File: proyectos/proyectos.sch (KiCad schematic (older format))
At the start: 54 parts, among them P1 CONN_01X06, P2 CONN_01X03, P3 CONN_01X05, P4 CONN_01X04, SW1 SW_PUSH, U1 AD8232_A, U2 ADP3339, U3 PIC16F688, Y1 Crystal_8MHz

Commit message: version ECG 1.4
INCORPORACION DE PIC Y REGULADOR
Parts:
- removed C8, C9: 1uF, Capacitors_SMD:C_0805_HandSoldering, symbol 1uF
- removed JP2, JP3, JP?: JUMPER, symbol JUMPER
- removed P1: CONN_01X06, Huellas:Pin_Header_Straight_1x06_Pitch2.54mm, symbol CONN_01X06
- removed P4: CONN_01X04, Pin_Headers:Pin_Header_Straight_1x04_Pitch2.54mm, symbol CONN_01X04
- removed R16, R17, R21, R25: 000, Resistors_SMD:R_0805_HandSoldering, symbol 000
- removed SW1: SW_PUSH, Huellas:SWICHT_KPT-1187B, symbol SW_PUSH
- removed U2: ADP3339, TO_SOT_Packages_SMD:SOT-223-3Lead_TabPin2, symbol ADP3339
- added C14, C9: 0.1uF, Capacitors_SMD:C_0805_HandSoldering, symbol 0.1uF
- added C15: 4.7uF, Capacitors_SMD:C_0805_HandSoldering, symbol 4.7uF
- added C8: 10uF, Capacitors_SMD:C_0805_HandSoldering, symbol 10uF
- added JP2: LATIDOS_ECG, Pin_Headers:Pin_Header_Straight_1x02_Pitch2.54mm, symbol LATIDOS_ECG
- added JP3: RESET_PIC, Pin_Headers:Pin_Header_Straight_1x02_Pitch2.54mm, symbol RESET_PIC
- added JP4: PASO_A/D, Pin_Headers:Pin_Header_Straight_1x02_Pitch2.54mm, symbol PASO_A/D
- added JP5: ALIMENT_PIC-KIT, Pin_Headers:Pin_Header_Straight_1x02_Pitch2.54mm, symbol ALIMENT_PIC-KIT
- added P1, P6: CONN_01X02, Pin_Headers:Pin_Header_Straight_1x02_Pitch2.54mm, symbol CONN_01X02
- added P4: CONN_01X03, Pin_Headers:Pin_Header_Straight_1x03_Pitch2.54mm, symbol CONN_01X03
- added P5: CONN_01X03, Huellas:Pin_Header_Straight_1x03_Pitch2.54mm, symbol CONN_01X03-RESCUE-proyectos
- added U2: ADP3303-3.3, Housings_SOIC:SOIC-8_3.9x4.9mm_Pitch1.27mm, symbol ADP3303-3.3
- JP1: value JUMPER3 -> ALIMEN_PIC; footprint (none) -> Pin_Headers:Pin_Header_Straight_1x03_Pitch2.54mm
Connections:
- net labels added: SDN_OFF, VCC, VCC_PIC
- net labels removed: 3V3, 3V_REG, Vpp
- wire segments 145 -> 147
- no-connect marks 0 -> 1
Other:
- note added: "ALIMENTACION\n"
- note added: "ANALOGICAS\n"
- note added: "DIGITALES\n"
- note added: "ENTRADA DE CONTROL\n DE APAGADO DEL ECG"
- note added: "IND. ALIMENTACION\n"
- note added: "OPCION DE ALIMENTACION DEL PIC\n\n"
- note added: "REGULADOR DE 3.3V\n"
- note added: "RESET"
- note removed: "IND. PIC16F688"
- note removed: "OPCION DE ALIMENTACION ECG\n"
- note removed: "REGULADOR DE 3V\n"
- note removed: "SALIDAS ANALOGICAS\n"
- moved on the sheet: C10, JP1, P2, P3, R19, R20, R22

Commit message: version ECG 1.5
MODIFICACION DE PAD TORNILLOS
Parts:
- P5: footprint Huellas:Pin_Header_Straight_1x03_Pitch2.54mm -> Pin_Headers:Pin_Header_Straight_1x03_Pitch2.54mm
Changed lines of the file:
@@
 F 0 "P5" H 4800 7450 50  0000 C CNN
 F 1 "CONN_01X03" V 4900 7250 50  0000 C CNN
-F 2 "Huellas:Pin_Header_Straight_1x03_Pitch2.54mm" H 4800 7250 50  0001 C CNN
+F 2 "Pin_Headers:Pin_Header_Straight_1x03_Pitch2.54mm" H 4800 7250 50  0001 C CNN
 F 3 "" H 4800 7250 50  0000 C CNN
 	1    4800 7250

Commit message: VERSION 1.7 ECG Y PIC
NUEVA VERSION
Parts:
- added P7, P8: CONN_01X01, Huellas:MountingHole_1.8mm_Pad, symbol CONN_01X01
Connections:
- net GND: now also P4.1 (P1); no longer P4.3 (P3)
- net O_DIG1: now also P4.2 (P2); no longer P4.1 (P1)
- net O_DIG2: now also P4.3 (P3); no longer P4.2 (P2)
- no-connect marks 1 -> 3
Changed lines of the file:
@@
 Text GLabel 8100 4250 0    47   Input ~ 0
 ADC
-Text Label 6250 6800 3    47   ~ 0
-GND
-Text Label 6350 6800 3    47   ~ 0
+Text Label 6450 6700 3    47   ~ 0
+GND
+Text Label 6250 6700 3    47   ~ 0
 O_DIG2
-Text Label 6450 6800 3    47   ~ 0
+Text Label 6350 6700 3    47   ~ 0
 O_DIG1
 Text Label 9950 3850 2    47   ~ 0
@@
 	9150 3550 9150 3700
 Wire Wire Line
-	6250 6950 6250 6800
-Wire Wire Line
-	6350 6950 6350 6800
-Wire Wire Line
-	6450 6950 6450 6800
+	6250 6700 6250 6950
+Wire Wire Line
+	6350 6700 6350 6950
+Wire Wire Line
+	6450 6700 6450 6950
 Wire Wire Line
 	8100 4400 7650 4400
@@
 	0    1    1    0
 $EndComp
+$Comp
+L CONN_01X01 P8
+U 1 1 591B656B
+P 10300 5900
+F 0 "P8" H 10300 6000 50  0000 C CNN
+F 1 "CONN_01X01" V 10400 5900 50  0000 C CNN
+F 2 "Huellas:MountingHole_1.8mm_Pad" H 10300 5900 50  0001 C CNN
+F 3 "" H 10300 5900 50  0000 C CNN
+	1    10300 5900
+	1    0    0    -1
+$EndComp
+$Comp
+L CONN_01X01 P7
+U 1 1 591B6624
+P 9350 5900
+F 0 "P7" H 9350 6000 50  0000 C CNN
+F 1 "CONN_01X01" V 9450 5900 50  0000 C CNN
+F 2 "Huellas:MountingHole_1.8mm_Pad" H 9350 5900 50  0001 C CNN
+F 3 "" H 9350 5900 50  0000 C CNN
+	1    9350 5900
+	1    0    0    -1
+$EndComp
+NoConn ~ 10100 5900
+NoConn ~ 9150 5900
 $EndSCHEMATC

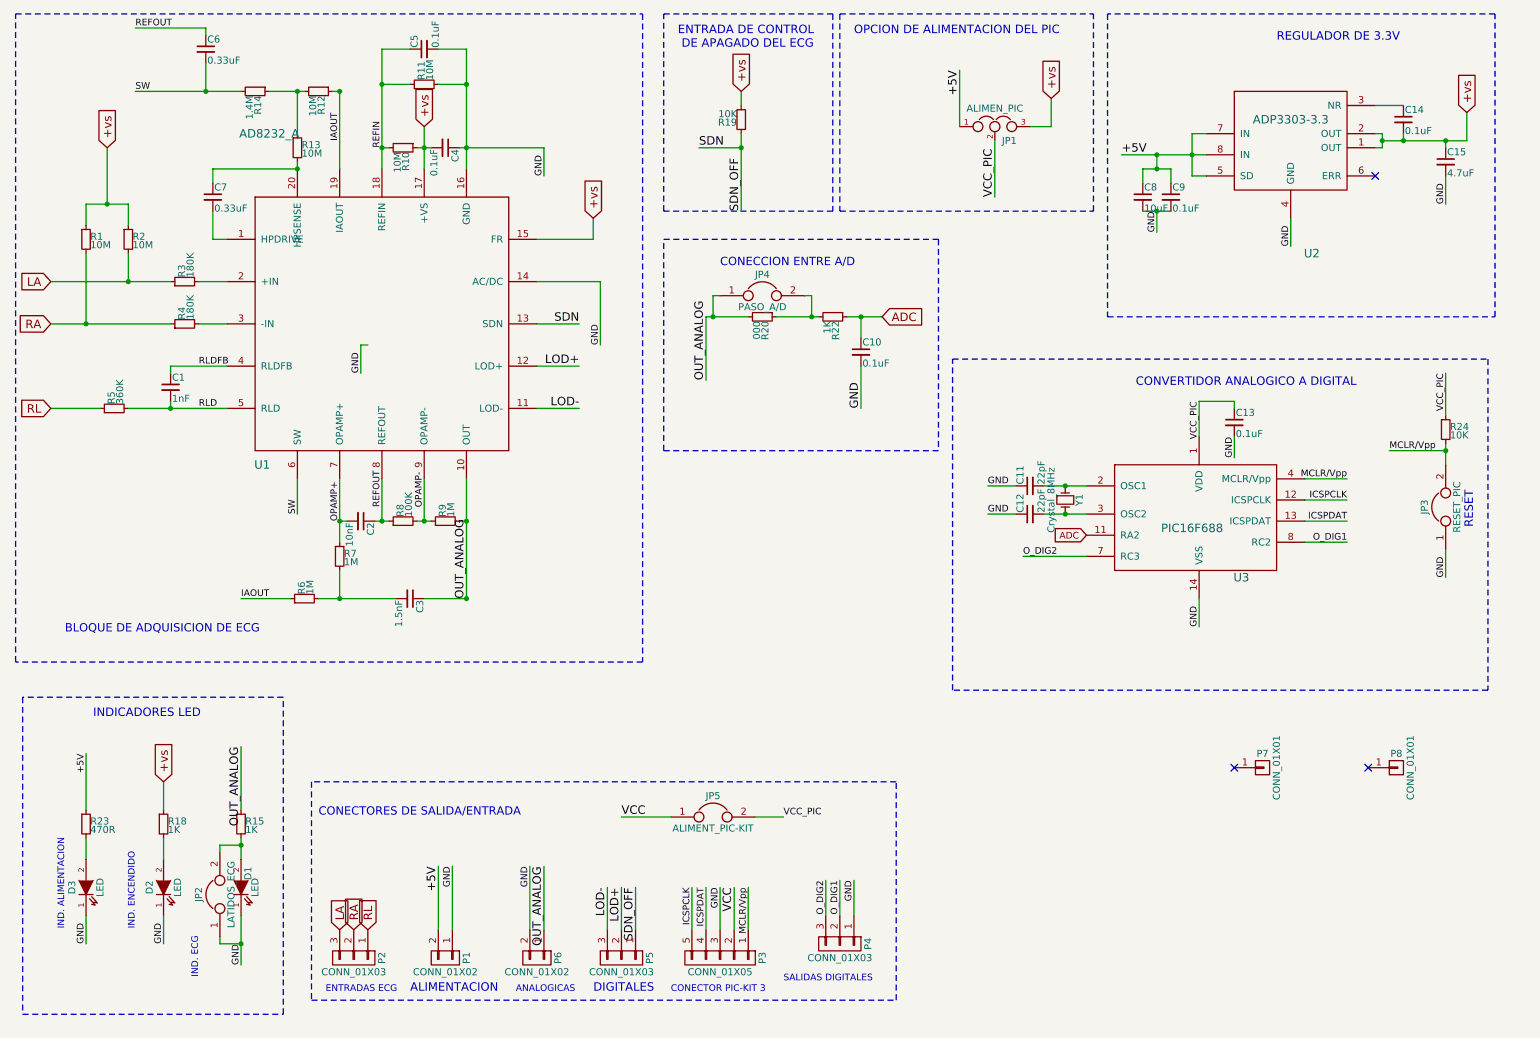
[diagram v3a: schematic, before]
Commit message: VERSION 1.8 ECG Y PIC
CAMBIO DE REGULADOR POR ADP3334
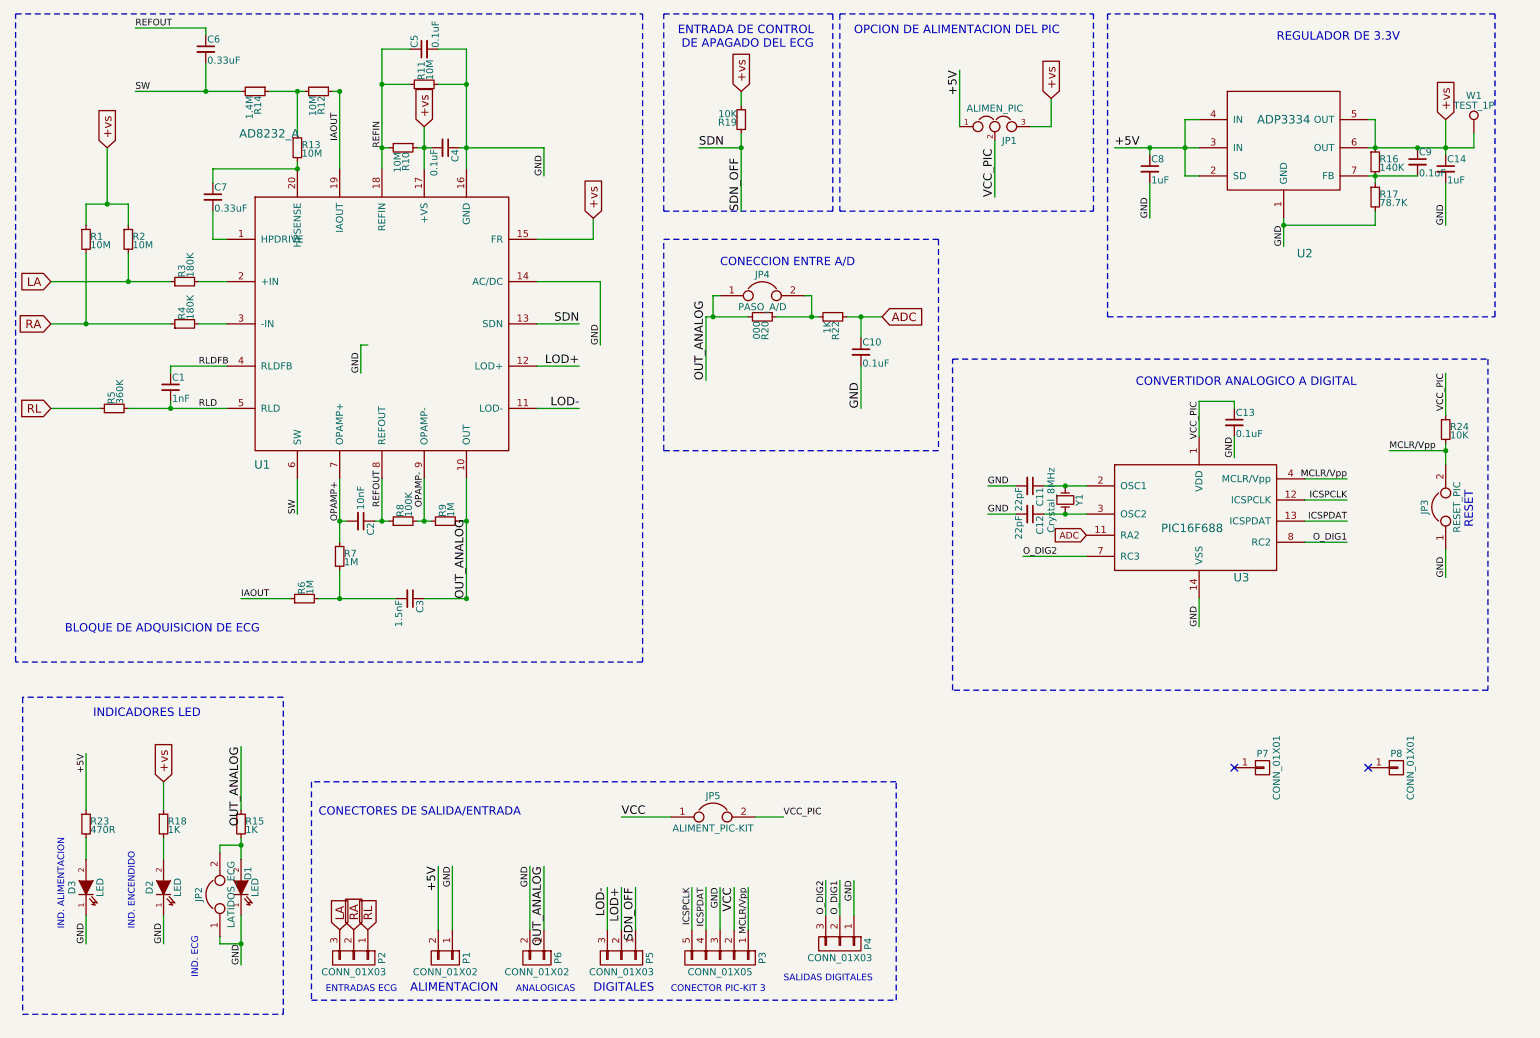
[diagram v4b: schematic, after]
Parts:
- removed C14: 0.1uF, Capacitors_SMD:C_0805_HandSoldering, symbol 0.1uF
- removed C15: 4.7uF, Capacitors_SMD:C_0805_HandSoldering, symbol 4.7uF
- removed C8: 10uF, Capacitors_SMD:C_0805_HandSoldering, symbol 10uF
- removed U2: ADP3303-3.3, Housings_SOIC:SOIC-8_3.9x4.9mm_Pitch1.27mm, symbol ADP3303-3.3
- added C14, C8: 1uF, Capacitors_SMD:C_0805_HandSoldering, symbol 1uF
- added R16: 140K, Resistors_SMD:R_0805_HandSoldering, symbol 140K
- added R17: 78.7K, Resistors_SMD:R_0805_HandSoldering, symbol 78.7K
- added U2: ADP3334, Housings_SOIC:SOIC-8_3.9x4.9mm_Pitch1.27mm, symbol ADP3334
- added W1: TEST_1P, Measurement_Points:Measurement_Point_Round-TH_Small, symbol TEST_1P
- C2: CAP CER 10000PF 50V X7R 0805 399-7363-2-ND -> 478-1383-2-ND
- Y1: CRYSTAL 8.0000MHZ 18PF SMD (none) -> 535-10630-2-ND
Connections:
- net +5V: now also C8.1, U2.2 (SD), U2.3 (IN), U2.4 (IN); no longer C9.1
- net +vs: now also C9.1, C14.1, R16.1, U2.5 (OUT), U2.6 (OUT), W1.1
- net GND: now also C11.2, C12.2, C14.2, C8.2, R17.2, U2.1 (GND); no longer C11.1, C12.1, C9.2
- net at U3.2 (OSC1), Y1.1: now also C11.1; no longer C11.2
- net at U3.3 (OSC2), Y1.2: now also C12.1; no longer C12.2
- new net: C9.2, R16.2, R17.1, U2.7 (FB)
- no-connect marks 3 -> 2
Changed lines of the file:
@@
 RLDFB
-$Comp
-L 10nF C2
-U 1 1 59135670
-P 2950 4150
-F 0 "C2" H 2960 4220 50  0000 L CNN
-F 1 "10nF" H 2960 4070 50  0000 L CNN
-F 2 "Capacitors_SMD:C_0805_HandSoldering" H 2860 4120 50  0001 C CNN
-F 3 "" H 2960 4220 50  0000 C CNN
-F 4 "399-7363-2-ND" H 3060 4320 60  0001 C CNN "CAP CER 10000PF 50V X7R 0805"
-	1    2950 4150
-	0    1    1    0
-$EndComp
 $Comp
 L 1.5nF C3
@@
 Text Label 5300 6750 3    47   ~ 0
 ICSPCLK
-$Comp
-L 22pF C11
-U 1 1 59128861
-P 7700 3900
-F 0 "C11" H 7710 3970 50  0000 L CNN
-F 1 "22pF" H 7710 3820 50  0000 L CNN
-F 2 "Capacitors_SMD:C_0805_HandSoldering" H 7610 3870 50  0001 C CNN
-F 3 "" H 7710 3970 50  0000 C CNN
-F 4 "399-1113-2-ND" H 7810 4070 60  0001 C CNN "CAP CER 22PF 50V C0G/NP0 0805"
-	1    7700 3900
-	0    -1   -1   0
-$EndComp
-$Comp
-L 22pF C12
-U 1 1 59128A52
-P 7700 4100
-F 0 "C12" H 7710 4170 50  0000 L CNN
-F 1 "22pF" H 7710 4020 50  0000 L CNN
-F 2 "Capacitors_SMD:C_0805_HandSoldering" H 7610 4070 50  0001 C CNN
-F 3 "" H 7710 4170 50  0000 C CNN
-F 4 "399-1113-2-ND" H 7810 4270 60  0001 C CNN "CAP CER 22PF 50V C0G/NP0 0805"
-	1    7700 4100
-	0    -1   -1   0
-$EndComp
 Text Label 7400 4100 0    47   ~ 0
 GND
@@
 Text Label 6500 3350 1    59   ~ 0
 GND
-Text Label 9550 2200 1    47   ~ 0
+Text Label 9500 2200 1    47   ~ 0
 GND
 Text Label 2950 3100 1    47   ~ 0
@@
 Text Label 3500 6600 3    60   ~ 0
 +5V
-Text Label 8350 1550 0    60   ~ 0
+Text Label 8300 1500 0    60   ~ 0
 +5V
 $Comp
@@
 Text Notes 10850 4200 1    60   ~ 0
 RESET
-Text Label 8600 2100 1    47   ~ 0
-GND
-NoConn ~ 10150 1700
-Text Label 10650 1900 1    47   ~ 0
-GND
-$Comp
-L 0.1uF C9
-U 1 1 5917A6BB
-P 8700 1850
-F 0 "C9" H 8710 1920 50  0000 L CNN
-F 1 "0.1uF" H 8710 1770 50  0000 L CNN
-F 2 "Capacitors_SMD:C_0805_HandSoldering" H 8610 1820 50  0001 C CNN
-F 3 "" H 8710 1920 50  0000 C CNN
-F 4 "1276-2450-2-ND" H 8810 2020 60  0001 C CNN "CAP CER 0.1UF 25V X7R 0805"
-	1    8700 1850
-	1    0    0    -1
-$EndComp
-$Comp
-L 0.1uF C14
-U 1 1 5917A9A4
-P 10350 1300
-F 0 "C14" H 10360 1370 50  0000 L CNN
-F 1 "0.1uF" H 10360 1220 50  0000 L CNN
-F 2 "Capacitors_SMD:C_0805_HandSoldering" H 10260 1270 50  0001 C CNN
-F 3 "" H 10360 1370 50  0000 C CNN
-F 4 "1276-2450-2-ND" H 10460 1470 60  0001 C CNN "CAP CER 0.1UF 25V X7R 0805"
-	1    10350 1300
-	1    0    0    -1
-$EndComp
-$Comp
-L 4.7uF C15
-U 1 1 5917AC64
-P 10650 1600
-F 0 "C15" H 10660 1670 50  0000 L CNN
-F 1 "4.7uF" H 10660 1520 50  0000 L CNN
-F 2 "Capacitors_SMD:C_0805_HandSoldering" H 10560 1570 50  0001 C CNN
-F 3 "" H 10660 1670 50  0000 C CNN
-F 4 "478-3280-2-ND" H 10760 1770 60  0001 C CNN "CAP TANT 4.7UF 10V 10% 080"
-	1    10650 1600
-	1    0    0    -1
-$EndComp
-$Comp
-L 10uF C8
-U 1 1 5917B51A
-P 8500 1850
-F 0 "C8" H 8510 1920 50  0000 L CNN
-F 1 "10uF" H 8510 1770 50  0000 L CNN
-F 2 "Capacitors_SMD:C_0805_HandSoldering" H 8410 1820 50  0001 C CNN
-F 3 "" H 8510 1920 50  0000 C CNN
-F 4 "511-1685-2-ND" H 8610 2020 60  0001 C CNN "CAP TANT 10UF 10V 20% 0805"
-	1    8500 1850
-	1    0    0    -1
-$EndComp
+Text Label 8550 2000 1    47   ~ 0
+GND
+Text Label 10650 2050 1    47   ~ 0
+GND
 Text Label 7450 1850 1    60   ~ 0
 VCC_PIC
@@
 DIGITALES\n
 $Comp
-L ADP3303-3.3 U2
-U 1 1 591A6799
-P 9550 1500
-F 0 "U2" H 9700 750 60  0000 C CNN
-F 1 "ADP3303-3.3" H 9550 1700 60  0000 C CNN
-F 2 "Housings_SOIC:SOIC-8_3.9x4.9mm_Pitch1.27mm" H 9450 1500 60  0001 C CNN
-F 3 "" H 9450 1500 60  0000 C CNN
-	1    9550 1500
-	1    0    0    -1
-$EndComp
-$Comp
 L AD8232_A U1
 U 1 1 591AD4B9
@@
 F 2 "Crystals:Crystal_SMD_Abracon_ABM3-2pin_5.0x3.2mm_HandSoldering" H 7850 4000 50  0001 C CNN
 F 3 "" H 7950 4100 50  0000 C CNN
+F 4 "535-10630-2-ND" H 7950 4000 60  0001 C CNN "CRYSTAL 8.0000MHZ 18PF SMD"
 	1    7950 4000
 	0    1    1    0
@@
 	4200 2750 4500 2750
 Wire Wire Line
-	9550 2200 9550 2000
+	9500 2200 9500 2000
 Wire Notes Line
 	8250 2700 11000 2700
@@
 Connection ~ 2100 7150
 Wire Wire Line
-	8850 1400 8850 1700
-Wire Wire Line
-	8850 1400 8950 1400
-Wire Wire Line
-	10150 1500 10200 1500
-Wire Wire Line
-	10200 1500 10200 1400
-Wire Wire Line
-	10200 1400 10150 1400
-Connection ~ 10200 1450
-Wire Wire Line
-	8850 1700 8950 1700
-Connection ~ 8850 1550
-Wire Wire Line
-	10350 1400 10350 1450
-Connection ~ 10350 1450
-Wire Wire Line
-	10350 1200 10150 1200
-Wire Wire Line
-	10650 1500 10650 1450
-Connection ~ 10650 1450
-Wire Wire Line
-	10650 1900 10650 1700
-Wire Wire Line
-	8500 1750 8500 1650
-Wire Wire Line
-	8500 1650 8700 1650
-Wire Wire Line
-	8600 1650 8600 1550
-Connection ~ 8600 1550
-Connection ~ 8600 1650
-Wire Wire Line
-	8500 1950 8700 1950
-Wire Wire Line
-	8600 1950 8600 2100
-Connection ~ 8600 1950
-Wire Wire Line
-	8700 1650 8700 1750
-Wire Wire Line
-	8950 1550 8350 1550
+	8800 1300 8800 1700
+Wire Wire Line
+	8800 1700 8900 1700
+Wire Wire Line
+	8550 1750 8550 2000
 Wire Notes Line
 	8250 550  8250 2700
@@
 Wire Wire Line
 	7850 1350 7850 1150
-Text GLabel 10800 1250 1    60   Input ~ 0
+Text GLabel 10650 1300 1    60   Input ~ 0
 +vs
-Wire Wire Line
-	10200 1450 10800 1450
-Wire Wire Line
-	10800 1450 10800 1250
 $Comp
 L CONN_01X02 P6
@@
 NoConn ~ 10100 5900
 NoConn ~ 9150 5900
+$Comp
+L 22pF C11
+U 1 1 591BBC5B
+P 7700 3900
+F 0 "C11" H 7710 3970 50  0000 L CNN
+F 1 "22pF" H 7710 3820 50  0000 L CNN
+F 2 "Capacitors_SMD:C_0805_HandSoldering" H 7610 3870 50  0001 C CNN
+F 3 "" H 7710 3970 50  0000 C CNN
+F 4 "399-1113-2-ND" H 7810 4070 60  0001 C CNN "CAP CER 22PF 50V C0G/NP0 0805"
+	1    7700 3900
+	0    1    1    0
+$EndComp
+$Comp
+L 22pF C12
+U 1 1 591BBD34
+P 7700 4100
+F 0 "C12" H 7710 4170 50  0000 L CNN
+F 1 "22pF" H 7710 4020 50  0000 L CNN
+F 2 "Capacitors_SMD:C_0805_HandSoldering" H 7610 4070 50  0001 C CNN
+F 3 "" H 7710 4170 50  0000 C CNN
+F 4 "399-1113-2-ND" H 7810 4270 60  0001 C CNN "CAP CER 22PF 50V C0G/NP0 0805"
+	1    7700 4100
+	0    1    1    0
+$EndComp
+$Comp
+L 10nF C2
+U 1 1 591C4351
+P 2950 4150
+F 0 "C2" H 2960 4220 50  0000 L CNN
+F 1 "10nF" H 2700 4150 50  0000 L CNN
+F 2 "Capacitors_SMD:C_0805_HandSoldering" H 2860 4120 50  0001 C CNN
+F 3 "" H 2960 4220 50  0000 C CNN
+F 4 "478-1383-2-ND" H 3060 4320 60  0001 C CNN "CAP CER 10000PF 50V X7R 0805"
+	1    2950 4150
+	0    1    1    0
+$EndComp
+$Comp
+L ADP3334 U2
+U 1 1 591DA311
+P 9500 1500
+F 0 "U2" H 9650 750 60  0000 C CNN
+F 1 "ADP3334" H 9500 1700 60  0000 C CNN
+F 2 "Housings_SOIC:SOIC-8_3.9x4.9mm_Pitch1.27mm" H 9800 2000 60  0001 C CNN
+F 3 "" H 9400 1500 60  0000 C CNN
+F 4 "ADP3334ARZ" H 9750 850 60  0001 C CNN "Adjustable Low Dropout Regulator "
+	1    9500 1500
+	1    0    0    -1
+$EndComp
+Wire Wire Line
+	8900 1300 8800 1300
+Wire Wire Line
+	8300 1500 8900 1500
+Connection ~ 8800 1500
+$Comp
+L 1uF C8
+U 1 1 591DE663
+P 8550 1650
+F 0 "C8" H 8560 1720 50  0000 L CNN
+F 1 "1uF" H 8560 1570 50  0000 L CNN
+F 2 "Capacitors_SMD:C_0805_HandSoldering" H 8460 1620 50  0001 C CNN
+F 3 "" H 8560 1720 50  0000 C CNN
+F 4 "1276-6495-2-ND" H 8660 1820 60  0001 C CNN "CAP CER 1UF 50V Y5V 0805"
+	1    8550 1650
+	1    0    0    -1
+$EndComp
+Wire Wire Line
+	8550 1550 8550 1500
+Connection ~ 8550 1500
+$Comp
+L 140K R16
+U 1 1 591E1018
+P 10150 1600
+F 0 "R16" H 10180 1620 50  0000 L CNN
+F 1 "140K" H 10180 1560 50  0000 L CNN
+F 2 "Resistors_SMD:R_0805_HandSoldering" H 10080 1520 50  0001 C CNN
+F 3 "" H 10180 1620 50  0000 C CNN
+F 4 "311-140KCRTR-ND" H 10280 1720 60  0001 C CNN "RES SMD 140K OHM 1% 1/8W 0805"
+	1    10150 1600
+	1    0    0    -1
+$EndComp
+$Comp
+L 78.7K R17
+U 1 1 591E182A
+P 10150 1850
+F 0 "R17" H 10180 1870 50  0000 L CNN
+F 1 "78.7K" H 10180 1810 50  0000 L CNN
+F 2 "Resistors_SMD:R_0805_HandSoldering" H 10080 1770 50  0001 C CNN
+F 3 "" H 10180 1870 50  0000 C CNN
+F 4 "311-78.7KCRTR-ND" H 10280 1970 60  0001 C CNN "RES SMD 78.7K OHM 1% 1/8W 0805"
+	1    10150 1850
+	1    0    0    -1
+$EndComp
+Connection ~ 10150 1500
+Wire Wire Line
+	10100 1300 10150 1300
+Wire Wire Line
+	10150 1300 10150 1500
+Wire Wire Line
+	10100 1700 10450 1700
+Wire Wire Line
+	10150 1700 10150 1750
+Wire Wire Line
+	10150 1950 10150 2050
+Wire Wire Line
+	10150 2050 9500 2050
+Connection ~ 9500 2050
+$Comp
+L 1uF C14
+U 1 1 591E2CB0
+P 10650 1650
+F 0 "C14" H 10660 1720 50  0000 L CNN
+F 1 "1uF" H 10660 1570 50  0000 L CNN
+F 2 "Capacitors_SMD:C_0805_HandSoldering" H 10560 1620 50  0001 C CNN
+F 3 "" H 10660 1720 50  0000 C CNN
+F 4 "1276-6495-2-ND" H 10760 1820 60  0001 C CNN "CAP CER 1UF 50V Y5V 0805"
+	1    10650 1650
+	1    0    0    -1
+$EndComp
+$Comp
+L 0.1uF C9
+U 1 1 591E6691
+P 10450 1600
+F 0 "C9" H 10460 1670 50  0000 L CNN
+F 1 "0.1uF" H 10460 1520 50  0000 L CNN
+F 2 "Capacitors_SMD:C_0805_HandSoldering" H 10360 1570 50  0001 C CNN
+F 3 "" H 10460 1670 50  0000 C CNN
+F 4 "1276-2450-2-ND" H 10560 1770 60  0001 C CNN "CAP CER 0.1UF 25V X7R 0805"
+	1    10450 1600
+	1    0    0    -1
+$EndComp
+Connection ~ 10450 1500
+Connection ~ 10150 1700
+Wire Wire Line
+	10650 1300 10650 1550
+Connection ~ 10650 1500
+$Comp
+L TEST_1P W1
+U 1 1 591DC131
+P 10850 1400
+F 0 "W1" H 10850 1670 50  0000 C CNN
+F 1 "TEST_1P" H 10850 1600 50  0000 C CNN
+F 2 "Measurement_Points:Measurement_Point_Round-TH_Small" H 11050 1400 50  0001 C CNN
+F 3 "" H 11050 1400 50  0000 C CNN
+	1    10850 1400
+	1    0    0    -1
+$EndComp
+Wire Wire Line
+	10100 1500 10850 1500
+Wire Wire Line
+	10850 1500 10850 1400
+Wire Wire Line
+	10650 2050 10650 1750
 $EndSCHEMATC
